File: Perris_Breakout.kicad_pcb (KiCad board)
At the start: 2 copper layers, 177.8 x 177.8 mm, 43 parts, among them J1 PERRI_1, J10 PERRI_10, J11 PERRI_11, J12 PERRI_12, J13 PERRI_13, J14 PERRI_14, J15 PERRI_15, J16 PERRI_16, J17 PERRI_17, J18 PERRI_18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

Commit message: All tracks complete. DRC passed with no errors or warnings.
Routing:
- net /SDA_2: track 111.0 -> 332.4 mm
- net /SCL_2: track 107.6 -> 302.5 mm
- net GND: track 0.00 -> 105.1 mm
- net /SCL_1: track 404.5 -> 388.3 mm
- net /SDA_1: track 357.2 -> 342.6 mm
- net /SCL_3: track 294.3 -> 288.6 mm
- net /SDA_3: track 276.7 -> 271.8 mm
- net +5V: track 171.7 -> 175.1 mm
- net /SCL_0: track 283.0 -> 281.8 mm
- net /SDA_0: track 340.0 -> 339.4 mm
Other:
- board text added: "Top"

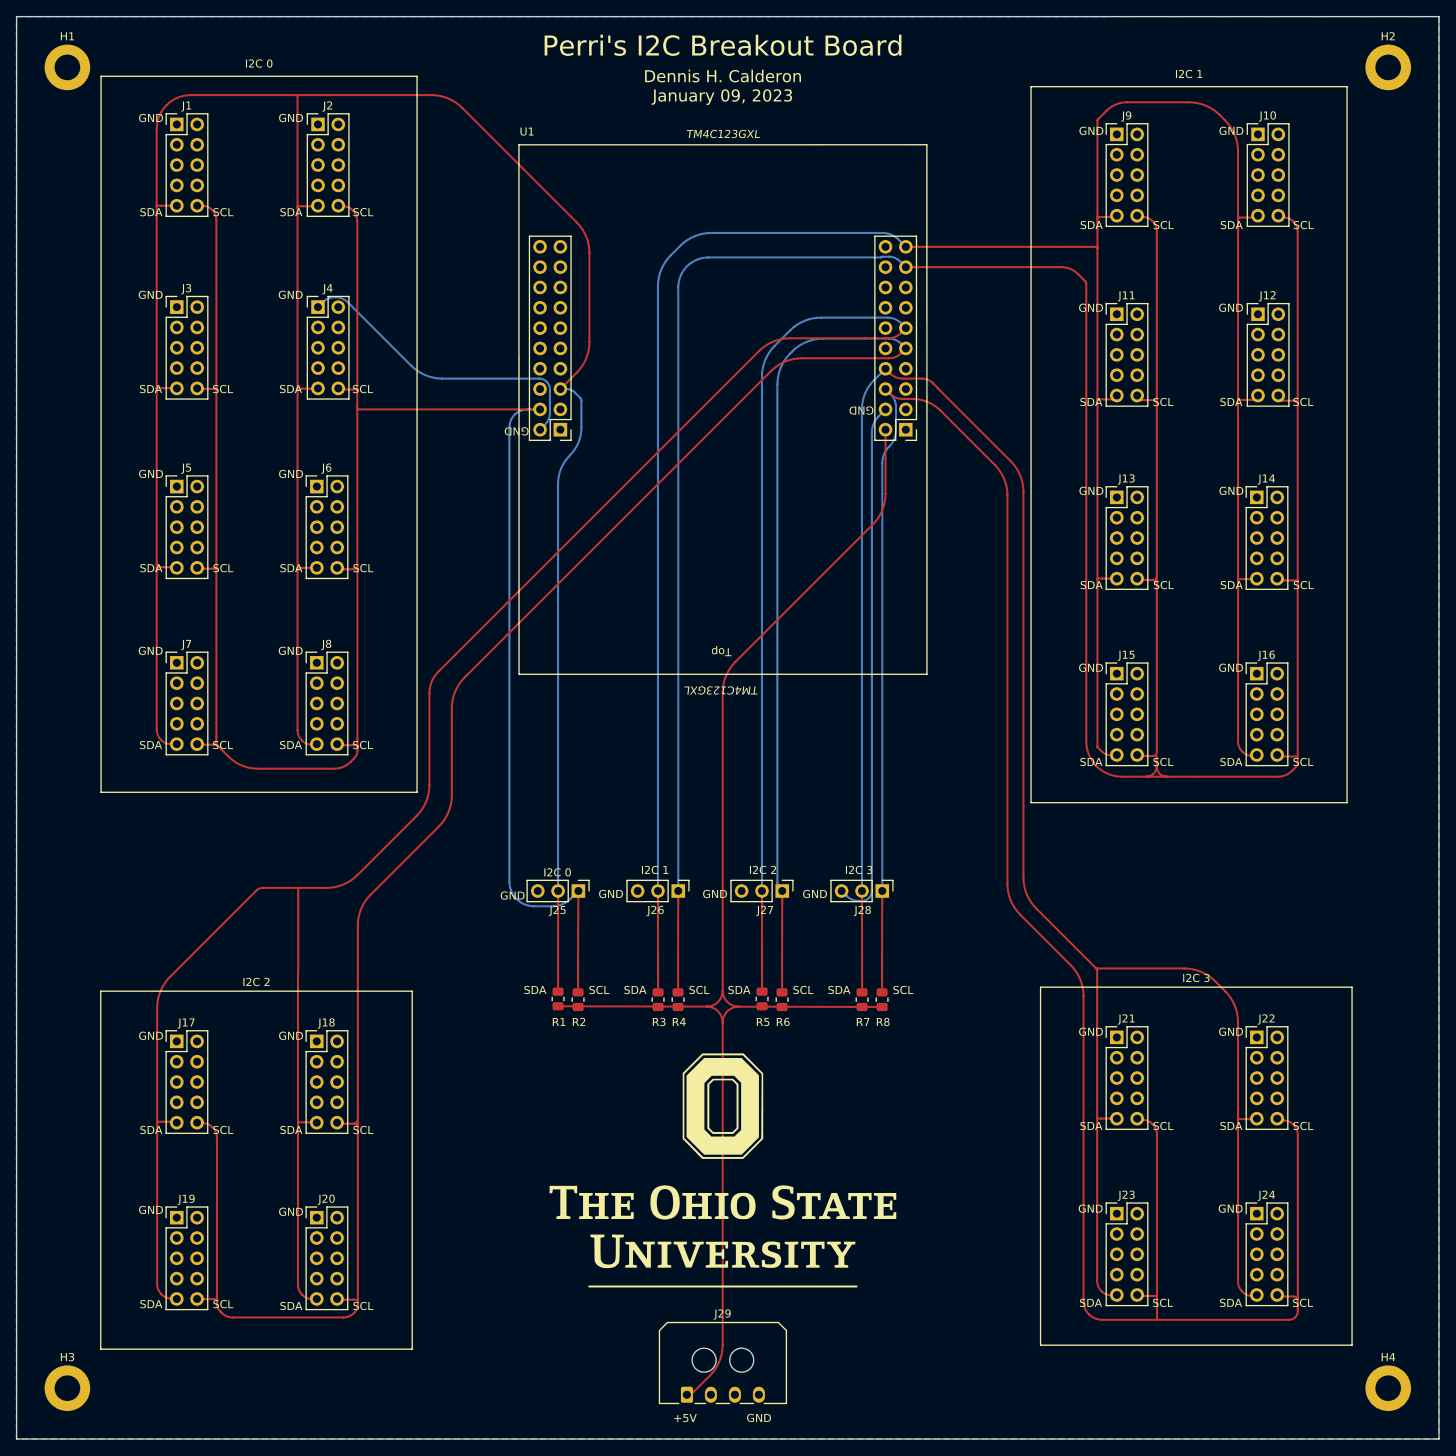
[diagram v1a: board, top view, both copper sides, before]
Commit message: Changed footprint for Perri connnector. Used vias. Fixed power connector orientation.
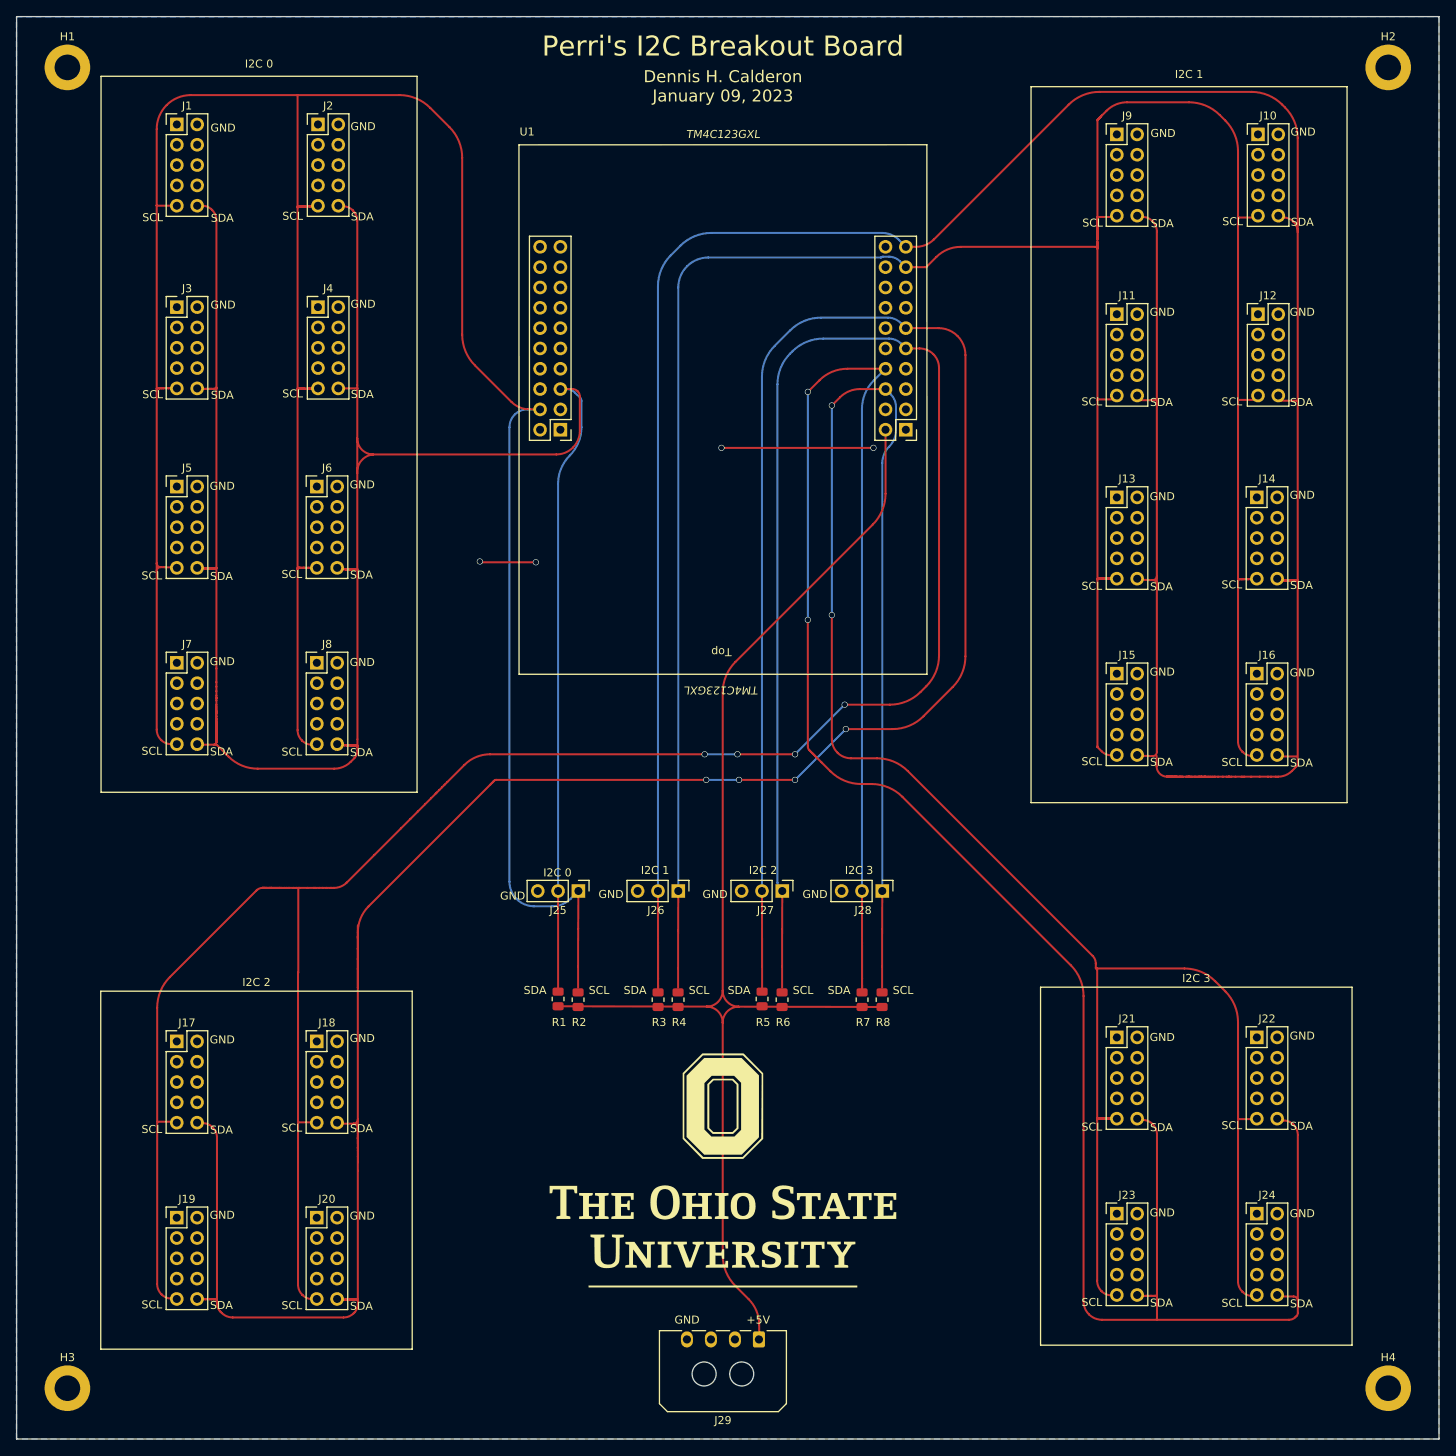
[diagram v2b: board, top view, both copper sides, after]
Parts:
- J1, J10, J11, J12, J13, J14, J15, J16, J17, J18, J19, J2, J20, J21, J22, J23, J24, J3, J4, J5, J6, J7, J8, J9: footprint HELIX:Perri_conn_2x5_Reverse -> HELIX:Perri_conn_2x5_CORRECT
- moved J29 11.4 mm to (111.5, 205.6), turned to 180 degrees
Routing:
- net GND: track 105.1 -> 26.0 mm, vias 0 -> 4
- net /SCL_0: track 281.8 -> 341.9 mm
- net /SCL_1: track 388.3 -> 338.0 mm
- net /SDA_0: track 339.4 -> 290.6 mm
- net /SCL_2: track 302.5 -> 350.2 mm, vias 0 -> 4
- net /SDA_3: track 271.8 -> 305.5 mm, vias 0 -> 2
- net /SDA_1: track 342.6 -> 369.0 mm
- net /SCL_3: track 288.6 -> 275.9 mm, vias 0 -> 2
- net /SDA_2: track 332.4 -> 344.5 mm, vias 0 -> 4
- net +5V: track 175.1 -> 167.8 mm

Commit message: Added silscreen to backside of board.
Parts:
- added G***: LOGO, LOGO, B.Cu at (111.2, 130.1)
